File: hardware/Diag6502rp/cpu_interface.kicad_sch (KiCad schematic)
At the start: 19 parts, among them J6 Conn_02x20_Counter_Clockwise, U4 TXS0108ERGYR, U5 TXS0108ERGYR, U6 TXS0108ERGYR, U7 TXS0108ERGYR, U8 TXS0108ERGYR

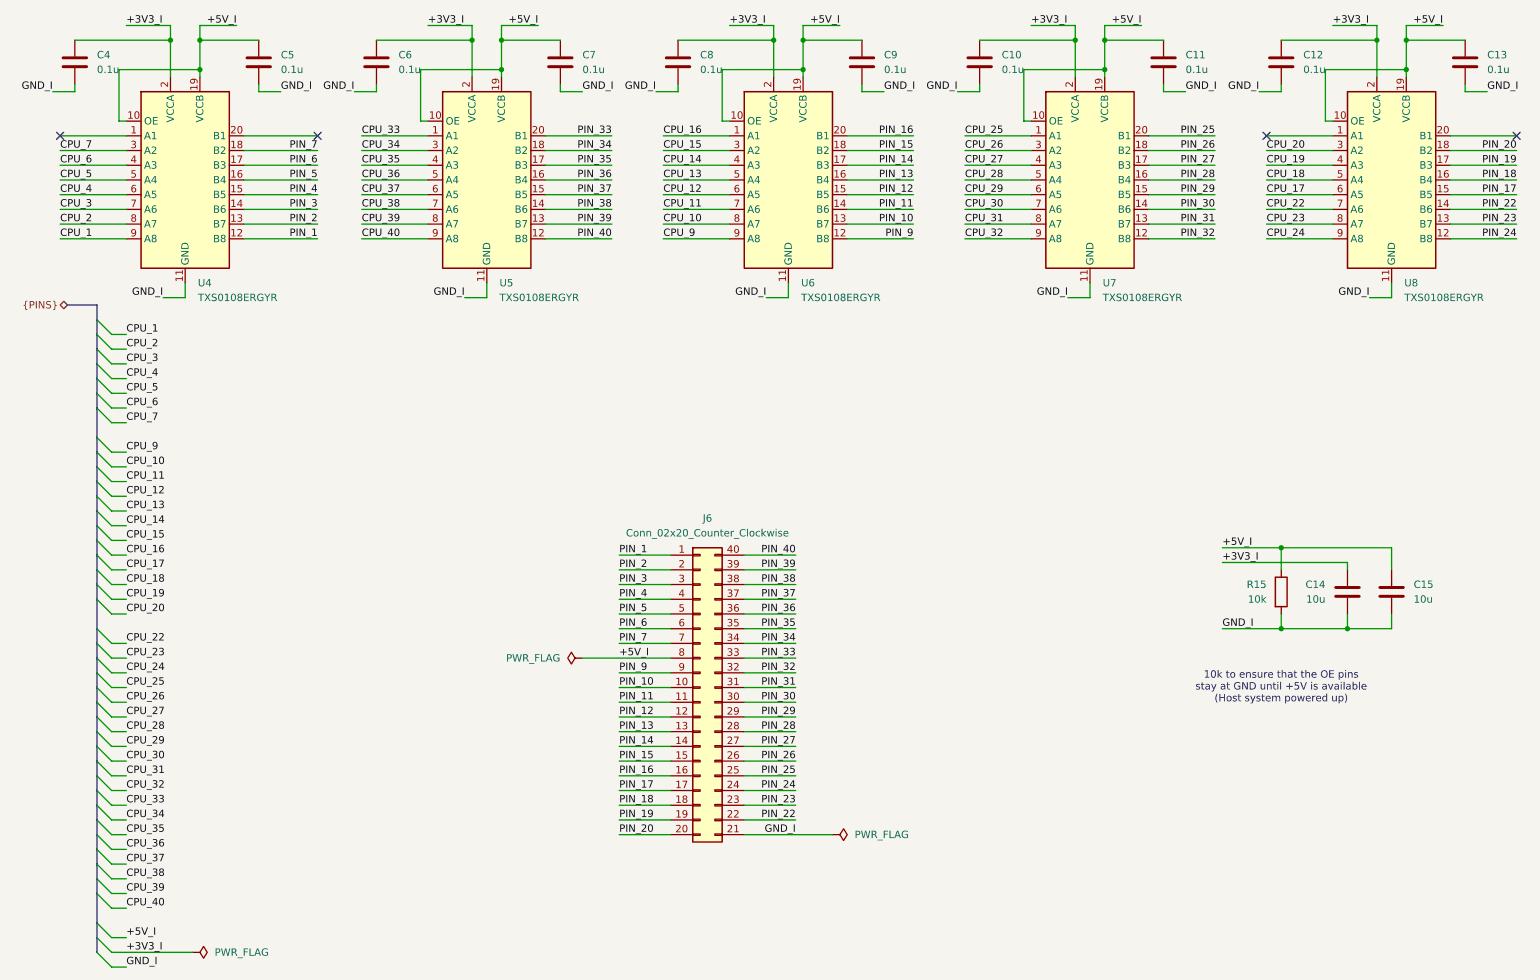
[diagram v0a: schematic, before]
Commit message: Changed TSX0108e foorprint to TSSOP20 for easier routing.
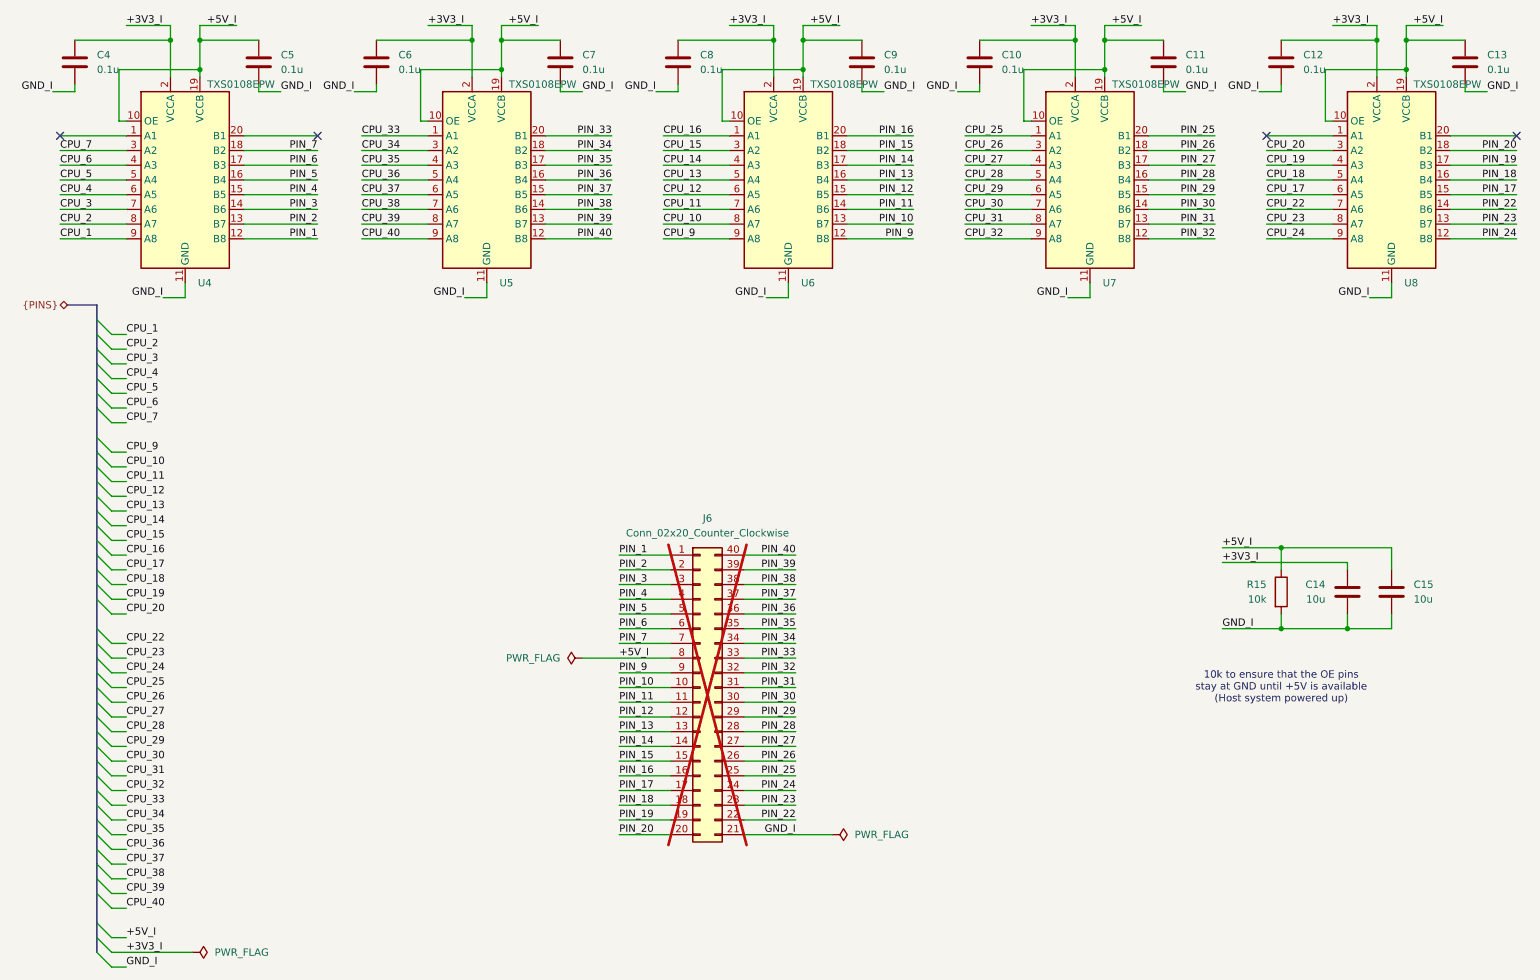
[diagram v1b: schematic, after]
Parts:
- J6: now not fitted
- U4, U5, U6, U7, U8: value TXS0108ERGYR -> TXS0108EPW; footprint footprints:IC_TXS0108ERGYR -> Package_SO:TSSOP-20_4.4x6.5mm_P0.65mm; symbol symbol_library:TXS0108ERGYR -> Logic_LevelTranslator:TXS0108EPW
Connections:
- net GND_I: no longer U4.21 (EP), U4.22 (EP_VIA), U4.23 (EP_VIA), U4.24 (EP_VIA), U4.25 (EP_VIA), U5.21 (EP), U5.22 (EP_VIA), U5.23 (EP_VIA), U5.24 (EP_VIA), U5.25 (EP_VIA), U6.21 (EP), U6.22 (EP_VIA), U6.23 (EP_VIA), U6.24 (EP_VIA), U6.25 (EP_VIA), U7.21 (EP), U7.22 (EP_VIA), U7.23 (EP_VIA), U7.24 (EP_VIA), U7.25 (EP_VIA), U8.21 (EP), U8.22 (EP_VIA), U8.23 (EP_VIA), U8.24 (EP_VIA), U8.25 (EP_VIA)
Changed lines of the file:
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@@
 	)
 	(symbol
-		(lib_id "symbol_library:TXS0108ERGYR")
+		(lib_id "Logic_LevelTranslator:TXS0108EPW")
 		(at 254 50.8 0)
 		(unit 1)
@@
 			)
 		)
-		(property "Value" "TXS0108ERGYR"
-			(at 256.1941 71.12 0)
-			(effects
-				(font
-					(size 1.27 1.27)
-				)
-				(justify left)
-			)
-		)
-		(property "Footprint" "footprints:IC_TXS0108ERGYR"
+		(property "Value" "TXS0108EPW"
+			(at 257.81 34.29 0)
+			(effects
+				(font
+					(size 1.27 1.27)
+				)
+				(justify left)
+			)
+		)
+		(property "Footprint" "Package_SO:TSSOP-20_4.4x6.5mm_P0.65mm"
 			(at 254 69.85 0)
 			(effects
@@
 			)
 		)
-		(property "Description" "Bidirectional  level-shifting voltage translator, VQFN"
+		(property "Description" "Bidirectional  level-shifting voltage translator, TSSOP-20"
 			(at 254 50.8 0)
 			(effects
@@
 			)
 		)
-		(pin "24"
-		)
 		(pin "16"
 		)
@@
 		(pin "7"
 		)
-		(pin "22"
-		)
 		(pin "13"
 		)
 		(pin "19"
 		)
-		(pin "23"
-		)
 		(pin "10"
 		)
@@
 		)
 		(pin "15"
-		)
-		(pin "21"
-		)
-		(pin "25"
 		)
 		(instances
@@
 	)
 	(symbol
-		(lib_id "symbol_library:TXS0108ERGYR")
+		(lib_id "Logic_LevelTranslator:TXS0108EPW")
 		(at 201.93 50.8 0)
 		(unit 1)
@@
 			)
 		)
-		(property "Value" "TXS0108ERGYR"
-			(at 204.1241 71.12 0)
-			(effects
-				(font
-					(size 1.27 1.27)
-				)
-				(justify left)
-			)
-		)
-		(property "Footprint" "footprints:IC_TXS0108ERGYR"
+		(property "Value" "TXS0108EPW"
+			(at 205.74 34.29 0)
+			(effects
+				(font
+					(size 1.27 1.27)
+				)
+				(justify left)
+			)
+		)
+		(property "Footprint" "Package_SO:TSSOP-20_4.4x6.5mm_P0.65mm"
 			(at 201.93 69.85 0)
 			(effects
@@
 			)
 		)
-		(property "Description" "Bidirectional  level-shifting voltage translator, VQFN"
+		(property "Description" "Bidirectional  level-shifting voltage translator, TSSOP-20"
 			(at 201.93 50.8 0)
 			(effects
@@
 			)
 		)
-		(pin "24"
-		)
 		(pin "16"
 		)
@@
 		(pin "7"
 		)
-		(pin "22"
-		)
 		(pin "13"
 		)
 		(pin "19"
 		)
-		(pin "23"
-		)
 		(pin "10"
 		)
@@
 		)
 		(pin "15"
-		)
-		(pin "21"
-		)
-		(pin "25"
 		)
 		(instances
@@
 	)
 	(symbol
-		(lib_id "symbol_library:TXS0108ERGYR")
+		(lib_id "Logic_LevelTranslator:TXS0108EPW")
 		(at 97.79 50.8 0)
 		(unit 1)
@@
 			)
 		)
-		(property "Value" "TXS0108ERGYR"
-			(at 99.9841 71.12 0)
-			(effects
-				(font
-					(size 1.27 1.27)
-				)
-				(justify left)
-			)
-		)
-		(property "Footprint" "footprints:IC_TXS0108ERGYR"
+		(property "Value" "TXS0108EPW"
+			(at 101.6 34.29 0)
+			(effects
+				(font
+					(size 1.27 1.27)
+				)
+				(justify left)
+			)
+		)
+		(property "Footprint" "Package_SO:TSSOP-20_4.4x6.5mm_P0.65mm"
 			(at 97.79 69.85 0)
 			(effects
@@
 			)
 		)
-		(property "Description" "Bidirectional  level-shifting voltage translator, VQFN"
+		(property "Description" "Bidirectional  level-shifting voltage translator, TSSOP-20"
 			(at 97.79 50.8 0)
 			(effects
@@
 			)
 		)
-		(pin "24"
-		)
 		(pin "16"
 		)
@@
 		(pin "7"
 		)
-		(pin "22"
-		)
 		(pin "13"
 		)
 		(pin "19"
 		)
-		(pin "23"
-		)
 		(pin "10"
 		)
@@
 		)
 		(pin "15"
-		)
-		(pin "21"
-		)
-		(pin "25"
 		)
 		(instances
@@
 		(in_bom yes)
 		(on_board yes)
-		(dnp no)
+		(dnp yes)
 		(fields_autoplaced yes)
 		(property "Reference" "J6"
@@
 	)
 	(symbol
-		(lib_id "symbol_library:TXS0108ERGYR")
+		(lib_id "Logic_LevelTranslator:TXS0108EPW")
 		(at 149.86 50.8 0)
 		(unit 1)
@@
 			)
 		)
-		(property "Value" "TXS0108ERGYR"
-			(at 152.0541 71.12 0)
-			(effects
-				(font
-					(size 1.27 1.27)
-				)
-				(justify left)
-			)
-		)
-		(property "Footprint" "footprints:IC_TXS0108ERGYR"
+		(property "Value" "TXS0108EPW"
+			(at 153.67 34.29 0)
+			(effects
+				(font
+					(size 1.27 1.27)
+				)
+				(justify left)
+			)
+		)
+		(property "Footprint" "Package_SO:TSSOP-20_4.4x6.5mm_P0.65mm"
 			(at 149.86 69.85 0)
 			(effects
@@
 			)
 		)
-		(property "Description" "Bidirectional  level-shifting voltage translator, VQFN"
+		(property "Description" "Bidirectional  level-shifting voltage translator, TSSOP-20"
 			(at 149.86 50.8 0)
 			(effects
@@
 			)
 		)
-		(pin "24"
-		)
 		(pin "16"
 		)
@@
 		(pin "7"
 		)
-		(pin "22"
-		)
 		(pin "13"
 		)
 		(pin "19"
 		)
-		(pin "23"
-		)
 		(pin "10"
 		)
@@
 		)
 		(pin "15"
-		)
-		(pin "21"
-		)
-		(pin "25"
 		)
 		(instances
@@
 	)
 	(symbol
-		(lib_id "symbol_library:TXS0108ERGYR")
+		(lib_id "Logic_LevelTranslator:TXS0108EPW")
 		(at 45.72 50.8 0)
 		(unit 1)
@@
 			)
 		)
-		(property "Value" "TXS0108ERGYR"
-			(at 47.9141 71.12 0)
-			(effects
-				(font
-					(size 1.27 1.27)
-				)
-				(justify left)
-			)
-		)
-		(property "Footprint" "footprints:IC_TXS0108ERGYR"
+		(property "Value" "TXS0108EPW"
+			(at 49.53 34.29 0)
+			(effects
+				(font
+					(size 1.27 1.27)
+				)
+				(justify left)
+			)
+		)
+		(property "Footprint" "Package_SO:TSSOP-20_4.4x6.5mm_P0.65mm"
 			(at 45.72 69.85 0)
 			(effects
@@
 			)
 		)
-		(property "Description" "Bidirectional  level-shifting voltage translator, VQFN"
+		(property "Description" "Bidirectional  level-shifting voltage translator, TSSOP-20"
 			(at 45.72 50.8 0)
 			(effects
@@
 			)
 		)
-		(pin "24"
-		)
 		(pin "16"
 		)
@@
 		(pin "7"
 		)
-		(pin "22"
-		)
 		(pin "13"
 		)
 		(pin "19"
 		)
-		(pin "23"
-		)
 		(pin "10"
 		)
@@
 		(pin "15"
 		)
-		(pin "21"
-		)
-		(pin "25"
-		)
-		(instances
+		(instances

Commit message: Main design completed
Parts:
- added J10, J11: Conn_01x20_Pin, Connector_PinHeader_2.54mm:PinHeader_1x20_P2.54mm_Vertical, symbol Connector:Conn_01x20_Pin
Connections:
- net +5V_I: now also J11.13 (Pin_13)
- net GND_I: now also J10.1 (Pin_1)
- net PIN_1: now also J11.20 (Pin_20)
- net PIN_10: now also J11.11 (Pin_11)
- net PIN_11: now also J11.10 (Pin_10)
- net PIN_12: now also J11.9 (Pin_9)
- net PIN_13: now also J11.8 (Pin_8)
- net PIN_14: now also J11.7 (Pin_7)
- net PIN_15: now also J11.6 (Pin_6)
- net PIN_16: now also J11.5 (Pin_5)
- net PIN_17: now also J11.4 (Pin_4)
- net PIN_18: now also J11.3 (Pin_3)
- net PIN_19: now also J11.2 (Pin_2)
- net PIN_2: now also J11.19 (Pin_19)
- net PIN_20: now also J11.1 (Pin_1)
- net PIN_22: now also J10.2 (Pin_2)
- net PIN_23: now also J10.3 (Pin_3)
- net PIN_24: now also J10.4 (Pin_4)
- net PIN_25: now also J10.5 (Pin_5)
- net PIN_26: now also J10.6 (Pin_6)
- net PIN_27: now also J10.7 (Pin_7)
- net PIN_28: now also J10.8 (Pin_8)
- net PIN_29: now also J10.9 (Pin_9)
- net PIN_3: now also J11.18 (Pin_18)
- net PIN_30: now also J10.10 (Pin_10)
- net PIN_31: now also J10.11 (Pin_11)
- net PIN_32: now also J10.12 (Pin_12)
- net PIN_33: now also J10.13 (Pin_13)
- net PIN_34: now also J10.14 (Pin_14)
- net PIN_35: now also J10.15 (Pin_15)
- net PIN_36: now also J10.16 (Pin_16)
- net PIN_37: now also J10.17 (Pin_17)
- net PIN_38: now also J10.18 (Pin_18)
- net PIN_39: now also J10.19 (Pin_19)
- net PIN_4: now also J11.17 (Pin_17)
- net PIN_40: now also J10.20 (Pin_20)
- net PIN_5: now also J11.16 (Pin_16)
- net PIN_6: now also J11.15 (Pin_15)
- net PIN_7: now also J11.14 (Pin_14)
- net PIN_9: now also J11.12 (Pin_12)
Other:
- note added: "CPU Socket"

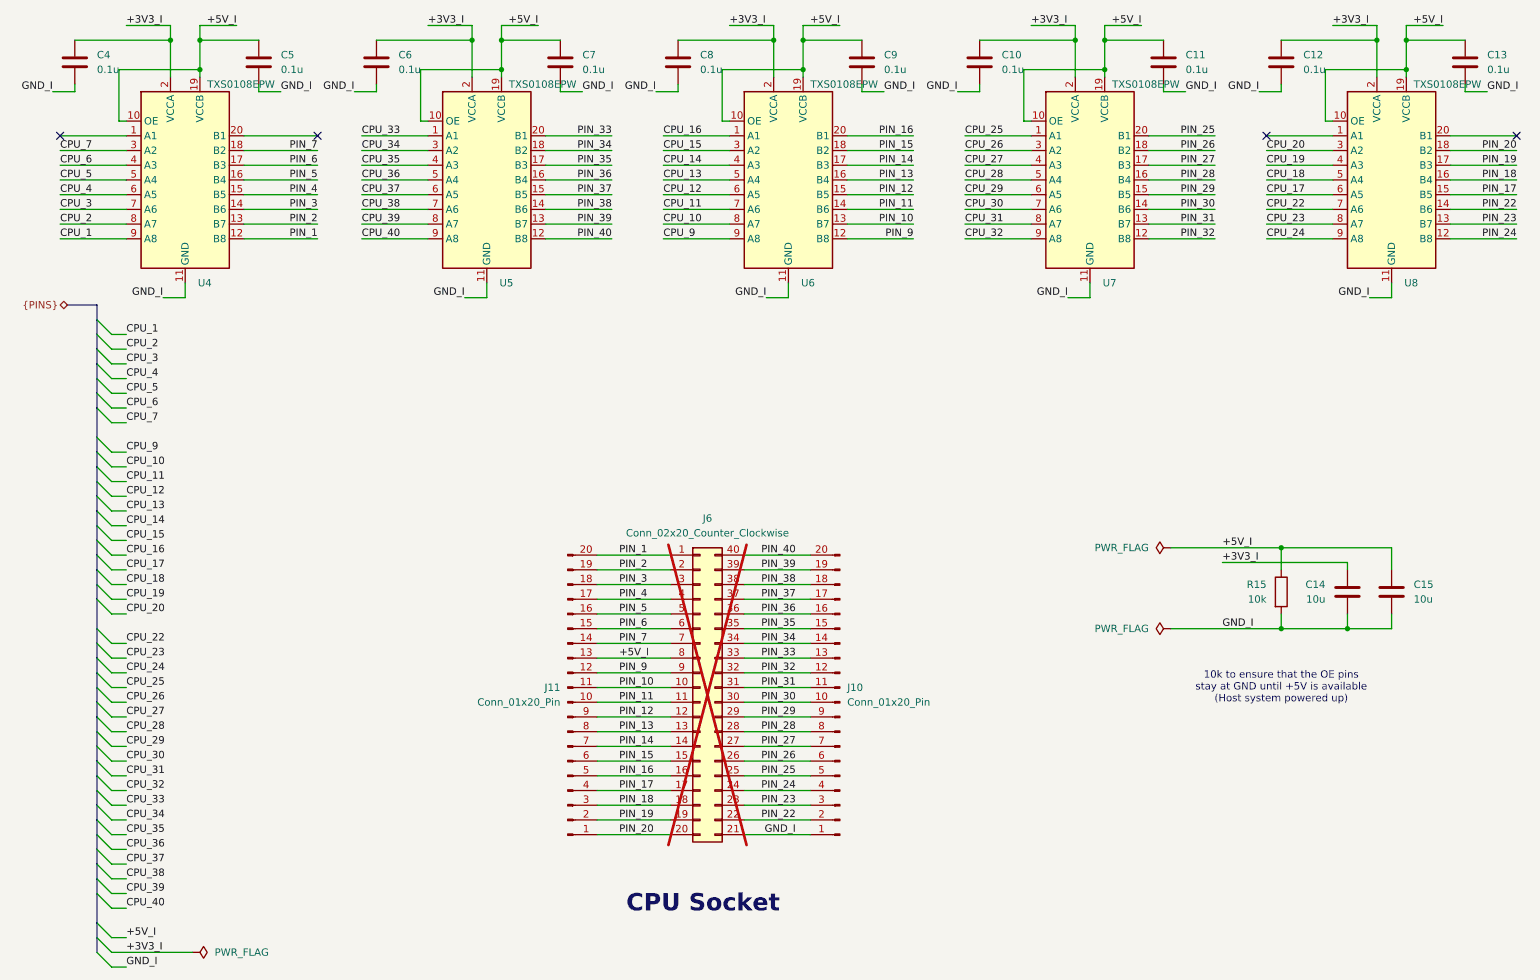
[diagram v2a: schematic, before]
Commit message: Cleanup, Fiduciaries, component spacing
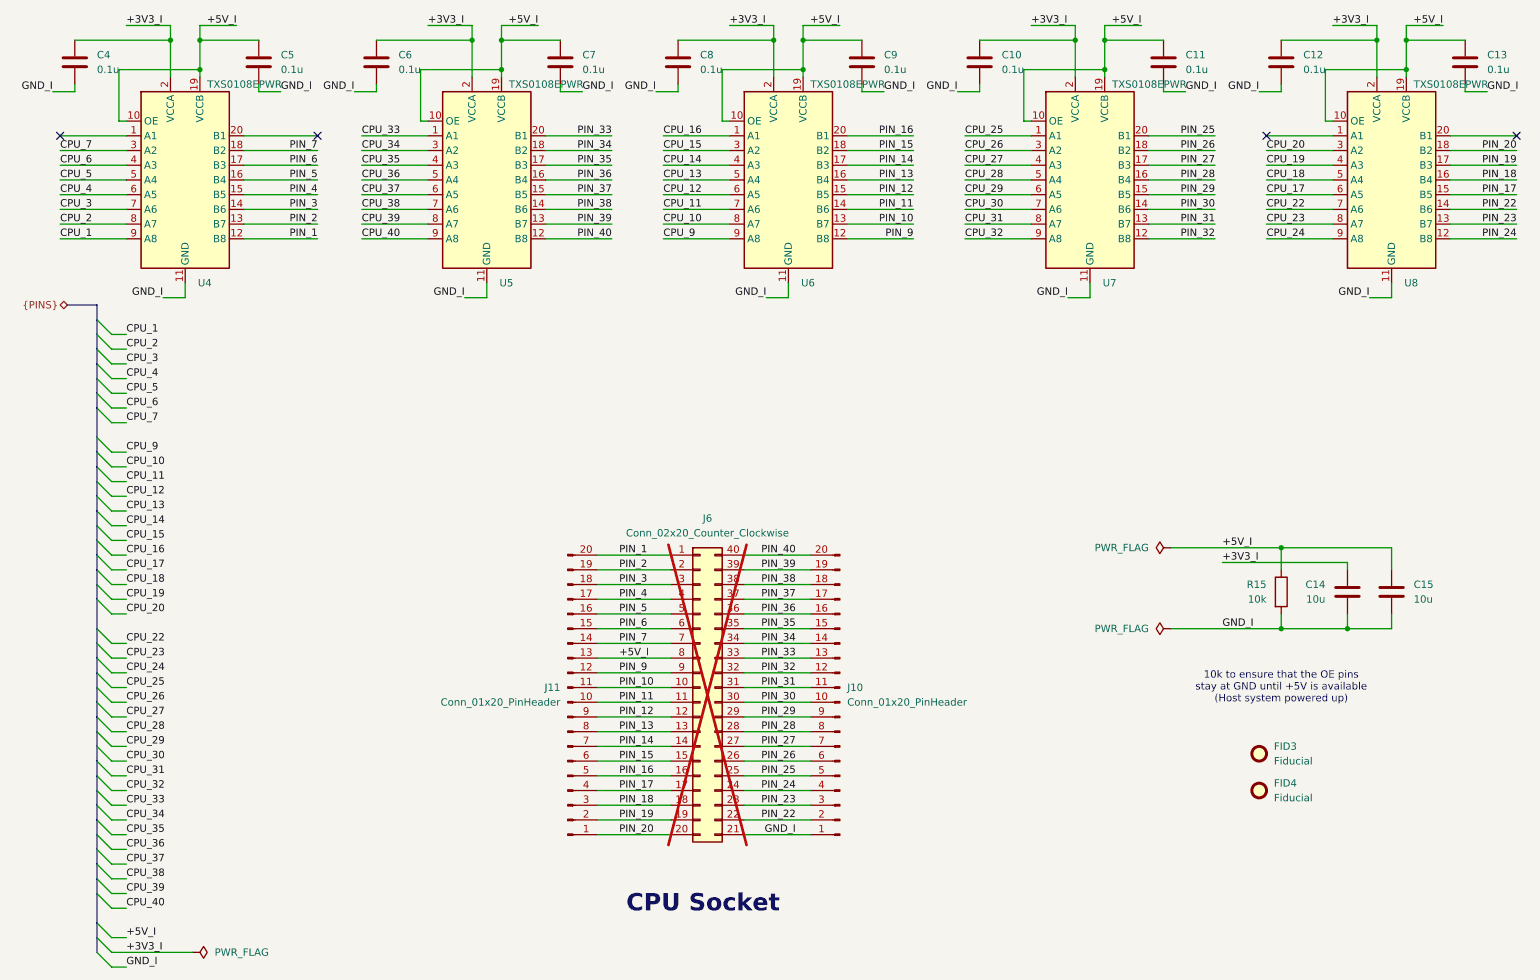
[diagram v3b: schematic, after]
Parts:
- added FID3, FID4: Fiducial, Fiducial:Fiducial_1mm_Mask2mm, symbol Mechanical:Fiducial
- C10, C11, C12, C13, C4, C5, C6, C7, C8, C9: footprint Capacitor_SMD:C_0402_1005Metric_Pad0.74x0.62mm_HandSolder -> Capacitor_SMD:C_0402_1005Metric; LCSC Part # (none) -> C1525
- C14, C15: footprint Capacitor_SMD:C_0603_1608Metric_Pad1.08x0.95mm_HandSolder -> Capacitor_SMD:C_0603_1608Metric; LCSC Part # (none) -> C19702
- J10, J11: value Conn_01x20_Pin -> Conn_01x20_PinHeader; LCSC Part # (none) -> C50981
- J6: now left out of the parts list
- R15: LCSC Part # (none) -> C25744
- U4, U5, U6, U7, U8: value TXS0108EPW -> TXS0108EPWR; LCSC Part # (none) -> C17206
